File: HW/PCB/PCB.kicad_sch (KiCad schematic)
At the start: 48 parts, among them J1 USB4105-GF-A, J2 DC_Jack, J4 Micro_SD_Card_Det_Hirose_DM3AT, Q1 2PC4081R, Q2 2PC4081R, SW1 ssss213202, SW2 SKRPACE010, SW3 SKRPACE010, U1 SCD40-D-R2, U2 FT231XS, U3 LT1963ES8-3.3, U4 ESP32-S3-WROOM-1, U5 BME280, U6 AQM0802A-RN-GBW, Y1 FC-135

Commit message: modify PCB layout
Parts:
- removed C11, C12: 0.1uF, Capacitor_SMD:C_0805_2012Metric_Pad1.18x1.45mm_HandSolder, symbol Device:C_Small
- removed U1: SCD40-D-R2, Sensor:Sensirion_SCD4x-1EP_10.1x10.1mm_P1.25mm_EP4.8x4.8mm, symbol Sensor_Gas:SCD40-D-R2
- removed U5: BME280, Package_LGA:Bosch_LGA-8_2.5x2.5mm_P0.65mm_ClockwisePinNumbering, symbol Sensor:BME280
- added H1, H2, H3, H4: M3_MountHoll, MountingHole:MountingHole_3.2mm_M3, symbol Mylib:MountHole_M3
- added U1: ~, mylib:BME280_SwitchScience, symbol Mylib:BME280_SwitchScience
- added U5: SCD40, mylib:SCD40_Conta, symbol Mylib:SCD40_SwitchScience
- C1, C2, C5: footprint Capacitor_SMD:C_0201_0603Metric_Pad0.64x0.40mm_HandSolder -> Capacitor_SMD:C_0603_1608Metric_Pad1.08x0.95mm_HandSolder
- R1, R2: footprint Resistor_SMD:R_0603_1608Metric_Pad0.98x0.95mm_HandSolder -> Resistor_SMD:R_1206_3216Metric_Pad1.30x1.75mm_HandSolder
- U4: footprint RF_Module:ESP32-S3-WROOM-1 -> mylib:ESP32-S3-WROOM-1
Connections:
- net +3V3: now also U1.4 (CSB), U1.6 (V_core), U1.7 (V_io), U5.5 (3V3)
- net ESP32_IO17_SCL: now also U1.2 (SCK), U5.1 (SCL)
- net ESP32_IO18_SDA: now also U1.3 (SDI), U5.2 (SDA)
- net GND: now also U1.1 (SDO), U1.5 (GND), U5.4 (GND)
- net VBUS: no longer names the net of J1.A4 (VBUS), J1.A9 (VBUS), J1.B4 (VBUS), J1.B9 (VBUS)
- no-connect marks 37 -> 39
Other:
- moved on the sheet: D4, D5, D6, R13, R14, R15

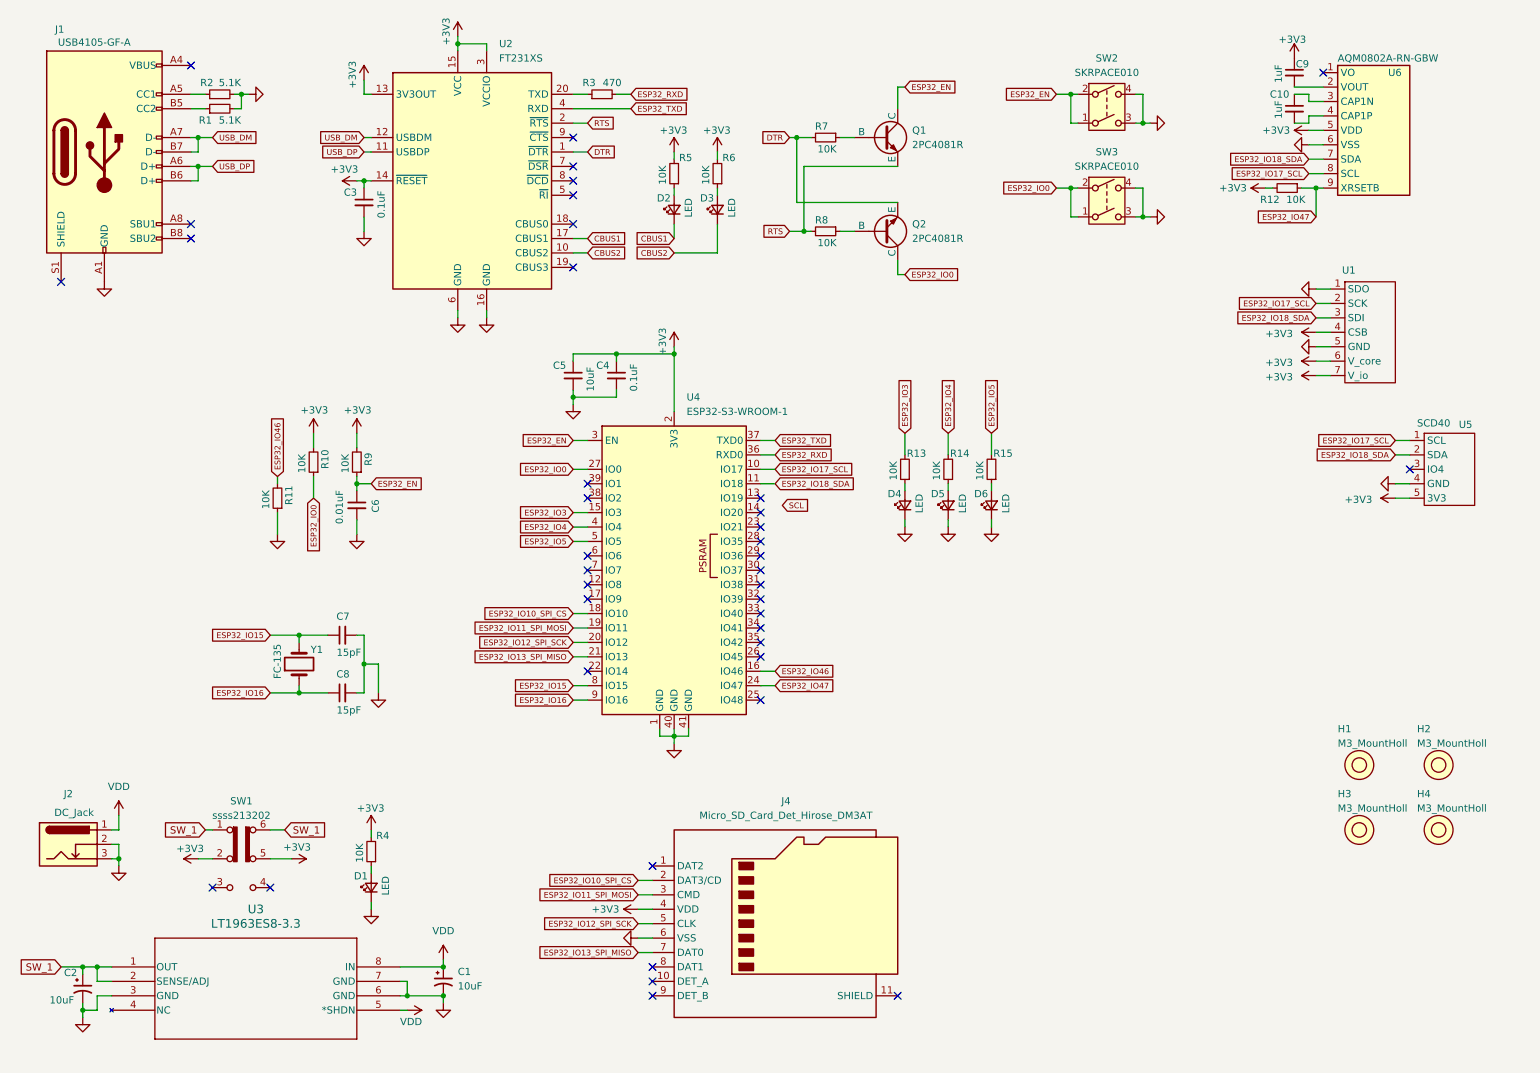
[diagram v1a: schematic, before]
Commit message: add PMIC
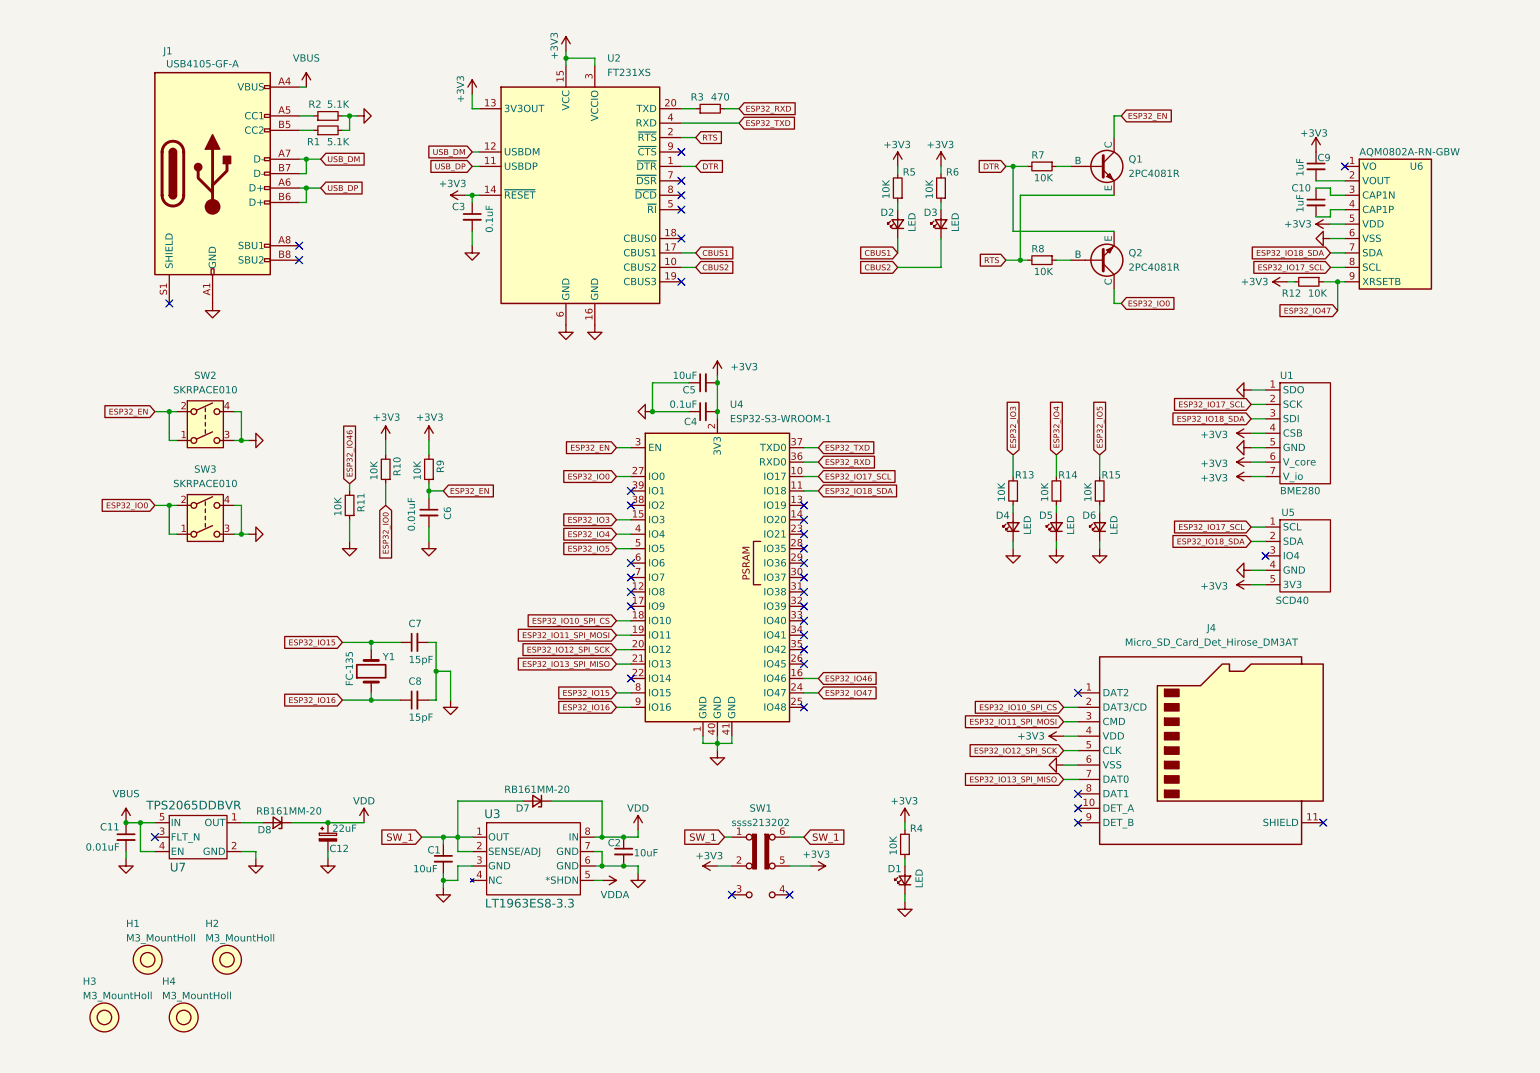
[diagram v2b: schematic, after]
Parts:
- removed C1, C2: 10uF, Capacitor_SMD:C_0603_1608Metric_Pad1.08x0.95mm_HandSolder, symbol Device:C_Polarized_Small_US
- removed J2: DC_Jack, mylib:MJ-179PH, symbol Connector:Barrel_Jack_Switch_Pin3Ring
- added C1, C2: 10uF, Capacitor_SMD:C_0603_1608Metric_Pad1.08x0.95mm_HandSolder, symbol Device:C_Small
- added C11: 0.01uF, Capacitor_SMD:C_0603_1608Metric_Pad1.08x0.95mm_HandSolder, symbol Device:C_Small
- added C12: 22uF, TAJ_SMD:TAJB_AVX, symbol Device:C_Polarized_Small
- added D7, D8: RB161MM-20, Diode_SMD:D_SOD-123, symbol Device:D_Zener_Small
- added U7: TPS2065DDBVR, Package_TO_SOT_SMD:SOT-23-5, symbol 2024-12-14_11-42-03:TPS2065DDBVR
- U1: value ~ -> BME280
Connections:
- net +3V3: now also C4.2, C5.2; no longer C4.1, C5.1
- net GND: now also C4.1, C5.1, C1.2, C11.2, C12.2, C2.2, U7.2 (GND); no longer C4.2, C5.2
- net SW_1: now also C1.1, D7.2 (A)
- net VDD: now also C12.1, C2.1, D7.1 (K), D8.1 (K); no longer U3.5 (*SHDN)
- net VBUS: now reaches J1.A4 (VBUS), J1.A9 (VBUS), J1.B4 (VBUS), J1.B9 (VBUS)
- net VBUS: now also C11.1, U7.4 (EN), U7.5 (IN)
- new net: D8.2 (A), U7.1 (OUT)
- new net VDDA: U3.5 (*SHDN)
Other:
- moved on the sheet: C10, C3, C4, C5, C6, C7, C8, C9, D1, D2, D3, D4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

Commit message: modify PCB design pattern
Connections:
- net VDDA is gone; now on net VDD: U3.5 (*SHDN)
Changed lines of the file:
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@@
+	)
+	(symbol
+		(lib_id "power:VDD")
+		(at 118.11 166.37 270)
+		(unit 1)
+		(exclude_from_sim no)
+		(in_bom yes)
+		(on_board yes)
+		(dnp no)
+		(property "Reference" "#PWR06"
+			(at 114.3 166.37 0)
+			(effects
+				(font
+					(size 1.27 1.27)
+				)
+				(hide yes)
+			)
+		)
+		(property "Value" "VDD"
+			(at 120.65 168.656 90)
+			(effects
+				(font
+					(size 1.27 1.27)
+				)
+			)
+		)
+		(property "Footprint" ""
+			(at 118.11 166.37 0)
+			(effects
+				(font
+					(size 1.27 1.27)
+				)
+				(hide yes)
+			)
+		)
+		(property "Datasheet" ""
+			(at 118.11 166.37 0)
+			(effects
+				(font
+					(size 1.27 1.27)
+				)
+				(hide yes)
+			)
+		)
+		(property "Description" "Power symbol creates a global label with name \"VDD\""
+			(at 118.11 166.37 0)
+			(effects
+				(font
+					(size 1.27 1.27)
+				)
+				(hide yes)
+			)
+		)
+		(pin "1"
+		)
+		(instances
+			(project "PCB"
+				(path "/f8d92c74-76e6-483a-a297-02aaf4ca0831"
+					(reference "#PWR06")
+					(unit 1)
+				)
+			)
+		)
 	)
 	(symbol
@@
 					(unit 1)
 				)
-			)
-		)
-	)
-	(symbol
-		(lib_id "power:VDDA")
-		(at 118.11 166.37 270)
-		(unit 1)
-		(exclude_from_sim no)
-		(in_bom yes)
-		(on_board yes)
-		(dnp no)
-		(property "Reference" "#PWR06"
-			(at 114.3 166.37 0)
-			(effects
-				(font
-					(size 1.27 1.27)
-				)
-				(hide yes)
-			)
-		)
-		(property "Value" "VDDA"
-			(at 117.856 168.91 90)
-			(effects
-				(font
-					(size 1.27 1.27)
-				)
-				(justify left)
-			)
-		)
-		(property "Footprint" ""
-			(at 118.11 166.37 0)
-			(effects
-				(font
-					(size 1.27 1.27)
-				)
-				(hide yes)
-			)
-		)
-		(property "Datasheet" ""
-			(at 118.11 166.37 0)
-			(effects
-				(font
-					(size 1.27 1.27)
-				)
-				(hide yes)
-			)
-		)
-		(property "Description" "Power symbol creates a global label with name \"VDDA\""
-			(at 118.11 166.37 0)
-			(effects
-				(font
-					(size 1.27 1.27)
-				)
-				(hide yes)
-			)
-		)
-		(pin "1"
-		)
-		(instances
-			(project "PCB"
-				(path "/f8d92c74-76e6-483a-a297-02aaf4ca0831"
-					(reference "#PWR06")
-					(unit 1)
-				)

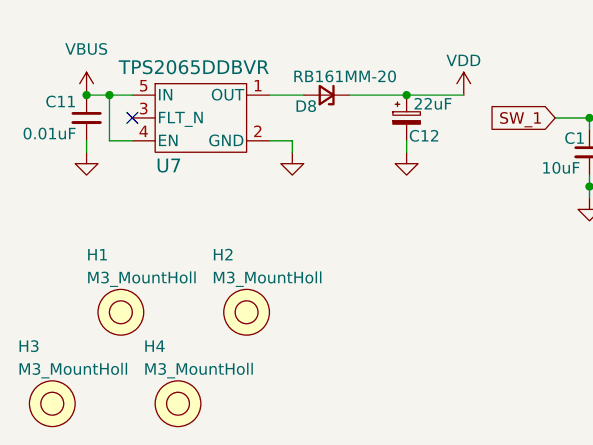
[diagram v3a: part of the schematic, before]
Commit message: modify PCB layout
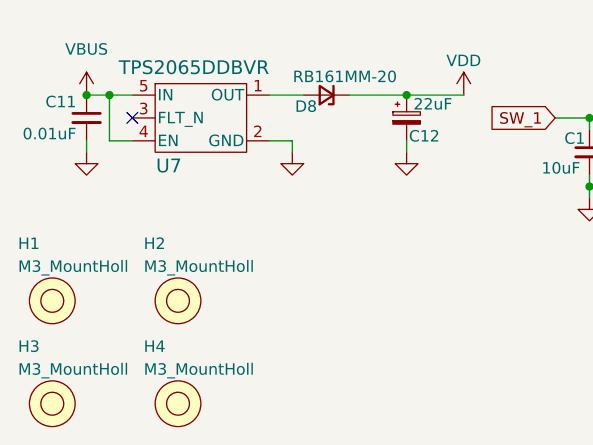
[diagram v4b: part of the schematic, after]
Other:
- moved on the sheet: H1, H2
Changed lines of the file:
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@@
 		(lib_name "MountHole_M3_1")
 		(lib_id "Mylib:MountHole_M3")
-		(at 38.1 180.34 0)
+		(at 30.48 179.07 0)
 		(unit 1)
 		(exclude_from_sim no)
@@
 		(fields_autoplaced yes)
 		(property "Reference" "H1"
-			(at 34.29 173.99 0)
+			(at 26.67 172.72 0)
 			(effects
 				(font
@@
 		)
 		(property "Value" "M3_MountHoll"
-			(at 34.29 176.53 0)
+			(at 26.67 175.26 0)
 			(effects
 				(font
@@
 		)
 		(property "Footprint" "MountingHole:MountingHole_3.2mm_M3"
-			(at 35.56 177.8 0)
+			(at 27.94 176.53 0)
 			(effects
 				(font
@@
 		)
 		(property "Datasheet" ""
-			(at 35.56 177.8 0)
+			(at 27.94 176.53 0)
 			(effects
 				(font
@@
 		)
 		(property "Description" ""
-			(at 35.56 177.8 0)
+			(at 27.94 176.53 0)
 			(effects
 				(font
@@
 		(lib_name "MountHole_M3_1")
 		(lib_id "Mylib:MountHole_M3")
-		(at 52.07 180.34 0)
+		(at 44.45 179.07 0)
 		(unit 1)
 		(exclude_from_sim no)
@@
 		(fields_autoplaced yes)
 		(property "Reference" "H2"
-			(at 48.26 173.99 0)
+			(at 40.64 172.72 0)
 			(effects
 				(font
@@
 		)
 		(property "Value" "M3_MountHoll"
-			(at 48.26 176.53 0)
+			(at 40.64 175.26 0)
 			(effects
 				(font
@@
 		)
 		(property "Footprint" "MountingHole:MountingHole_3.2mm_M3"
-			(at 49.53 177.8 0)
+			(at 41.91 176.53 0)
 			(effects
 				(font
@@
 		)
 		(property "Datasheet" ""
-			(at 49.53 177.8 0)
+			(at 41.91 176.53 0)
 			(effects
 				(font
@@
 		)
 		(property "Description" ""
-			(at 49.53 177.8 0)
-			(effects
-				(font
+			(at 41.91 176.53 0)
+			(effects
+				(font
